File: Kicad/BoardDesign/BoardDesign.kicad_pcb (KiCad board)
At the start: 4 copper layers, 33.1 x 53 mm, 38 parts, among them IC1 HX717, IC2 RT9080-33GJ5, J1 Conn_01x04_Socket, J2 USB_C_Receptacle_USB2.0_16P, J3 Conn_01x04_Socket, J4 Conn_01x04_Socket, SW1 SW_SPST, SW2 SW_SPST, SW3 SW_SPST, SW4 SW_SPST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

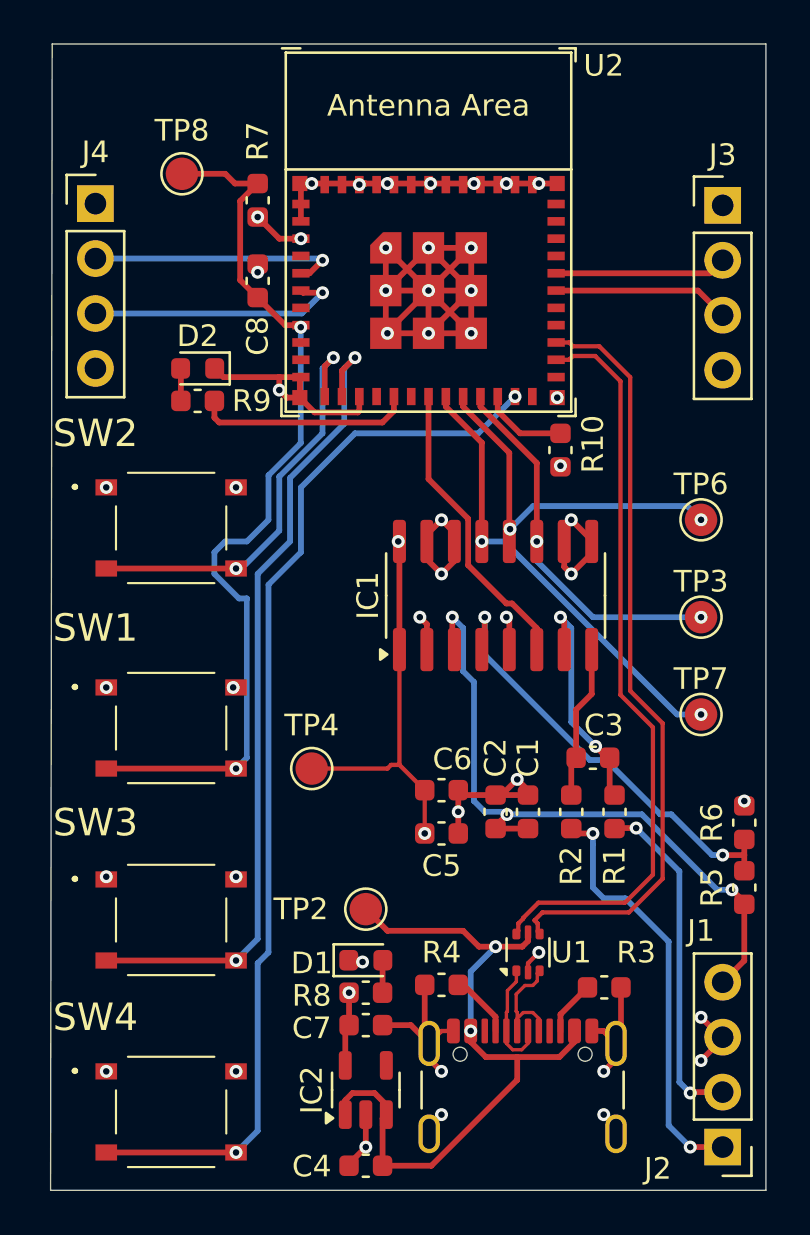
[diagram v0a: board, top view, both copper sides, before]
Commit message: Diseño placa semi terminado
Faltan un par de footprints
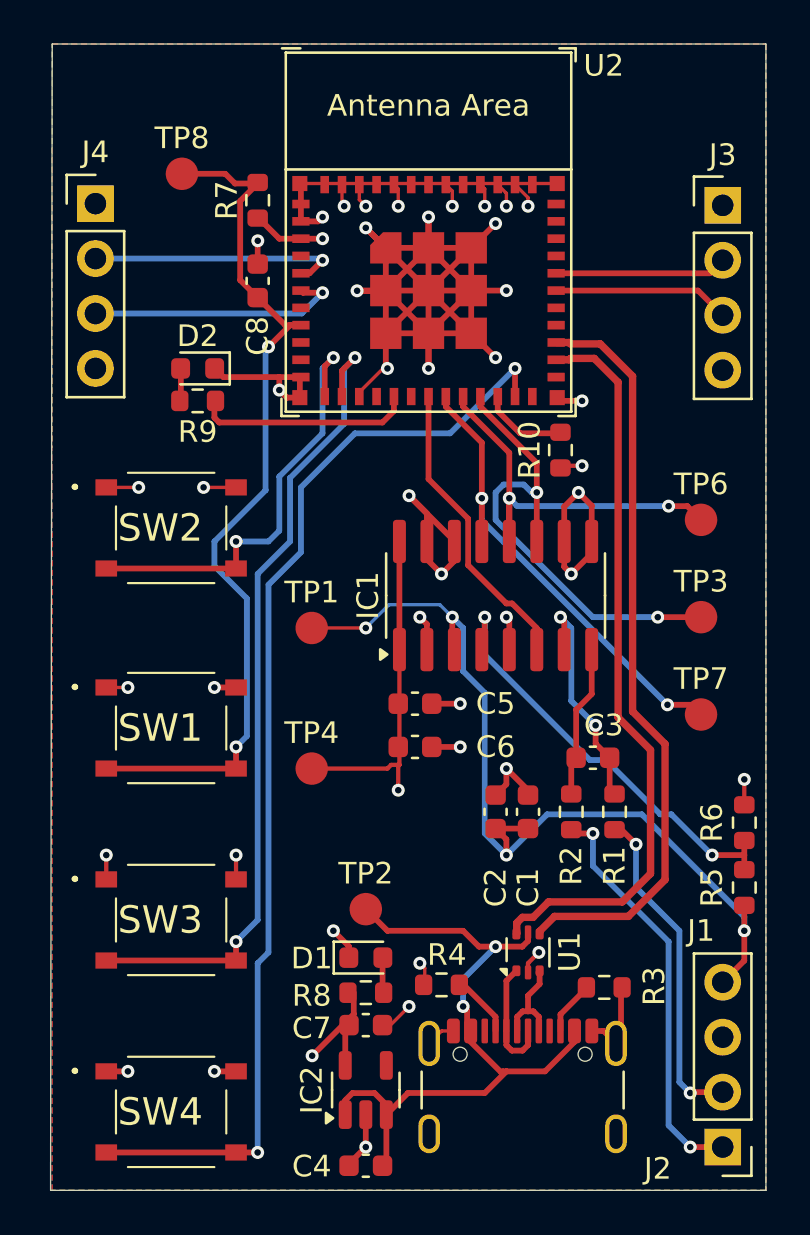
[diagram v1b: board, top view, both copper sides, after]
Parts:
- added TP1: TestPoint, custom_footprints:TestPoint_Pad_D1.5mm_nosilk, F.Cu at (136.5, 104.5)
- R1, R10, R2, R3, R4, R5, R6, R7, R8, R9: footprint Capacitor_SMD:C_0603_1608Metric -> Resistor_SMD:R_0603_1608Metric
- TP2, TP3, TP4, TP6, TP7, TP8: footprint TestPoint:TestPoint_Pad_D1.5mm -> custom_footprints:TestPoint_Pad_D1.5mm_nosilk
- moved C5 6.12 mm to (141.3, 108.0)
- moved C6 2.35 mm to (141.3, 110.0)
- moved D1 0.12 mm to (139.0, 119.7)
- turned TP4 to 0 degrees
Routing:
- net GND: track 114.0 -> 156.2 mm, vias 45 -> 42
- net +3V3: track 81.3 -> 106.9 mm, vias 6 -> 4
- net Net-(IC1-VRO/VREF): track 31.4 -> 42.1 mm, vias 3 -> 4
- net PD_SCK: track 17.4 -> 22.6 mm
- net Net-(SW4-B): track 49.6 -> 52.1 mm
- net /VBUS: track 34.2 -> 32.6 mm
- net S1: track 20.8 -> 22.3 mm
- net DOUT: track 17.7 -> 18.9 mm
- net Net-(SW1-B): track 41.9 -> 40.9 mm
- net DIN+: track 5.85 -> 4.85 mm
- net Net-(SW2-B): track 19.7 -> 20.5 mm
- net Net-(J1-Pin_1): track 19.5 -> 19.0 mm
- added copper zone on B.Cu, net GND
- added copper zone on F.Cu, net GND
- added copper zone on In1.Cu, net GND
